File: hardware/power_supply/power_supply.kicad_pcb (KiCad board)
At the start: 2 copper layers, 163 x 130 mm, 168 parts, among them P101 XFRMR, P102 Clock board, P103 Rx #1, P104 Rx #2, P105 CPU board, Q201 IRLZ44N, Q202 BC547, Q203 BC557, Q301 IRFZ34N, Q302 IRF9Z34N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

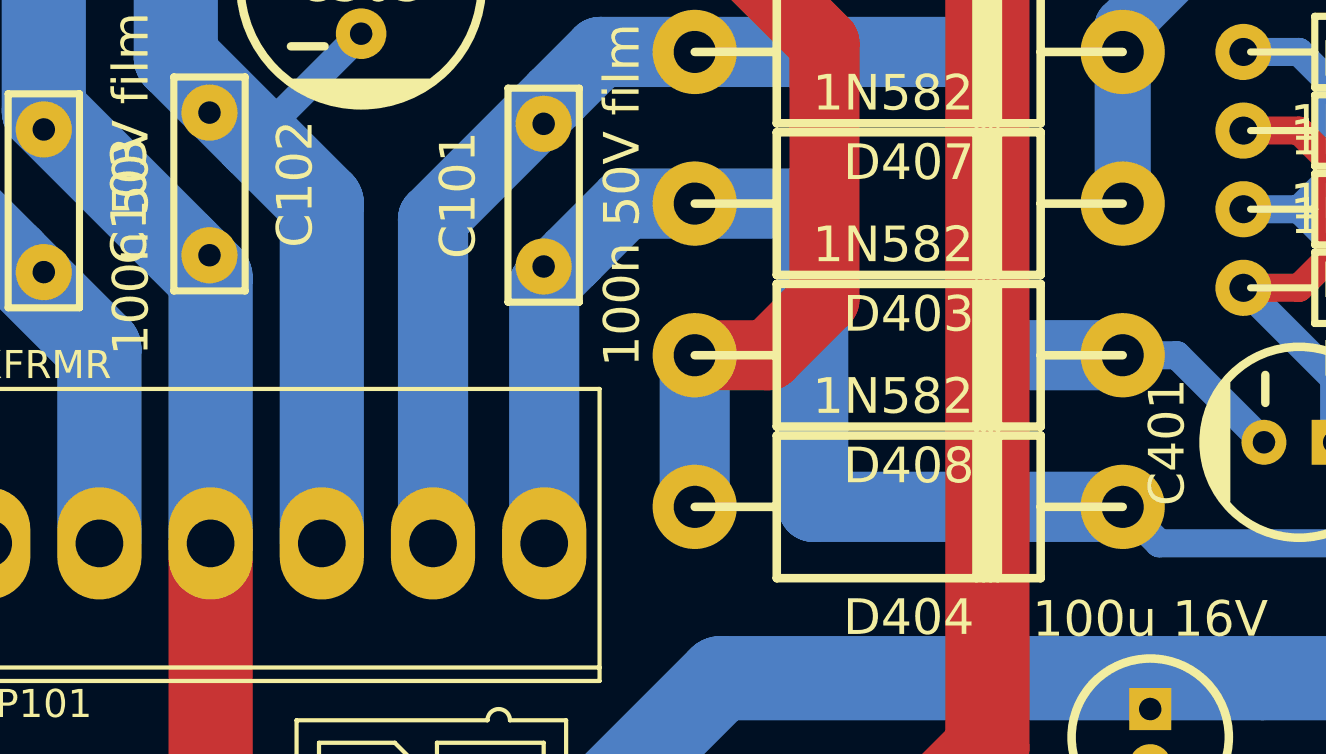
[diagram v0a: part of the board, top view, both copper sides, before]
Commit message: Update: PCB gerbers, images. Tagged v0.15
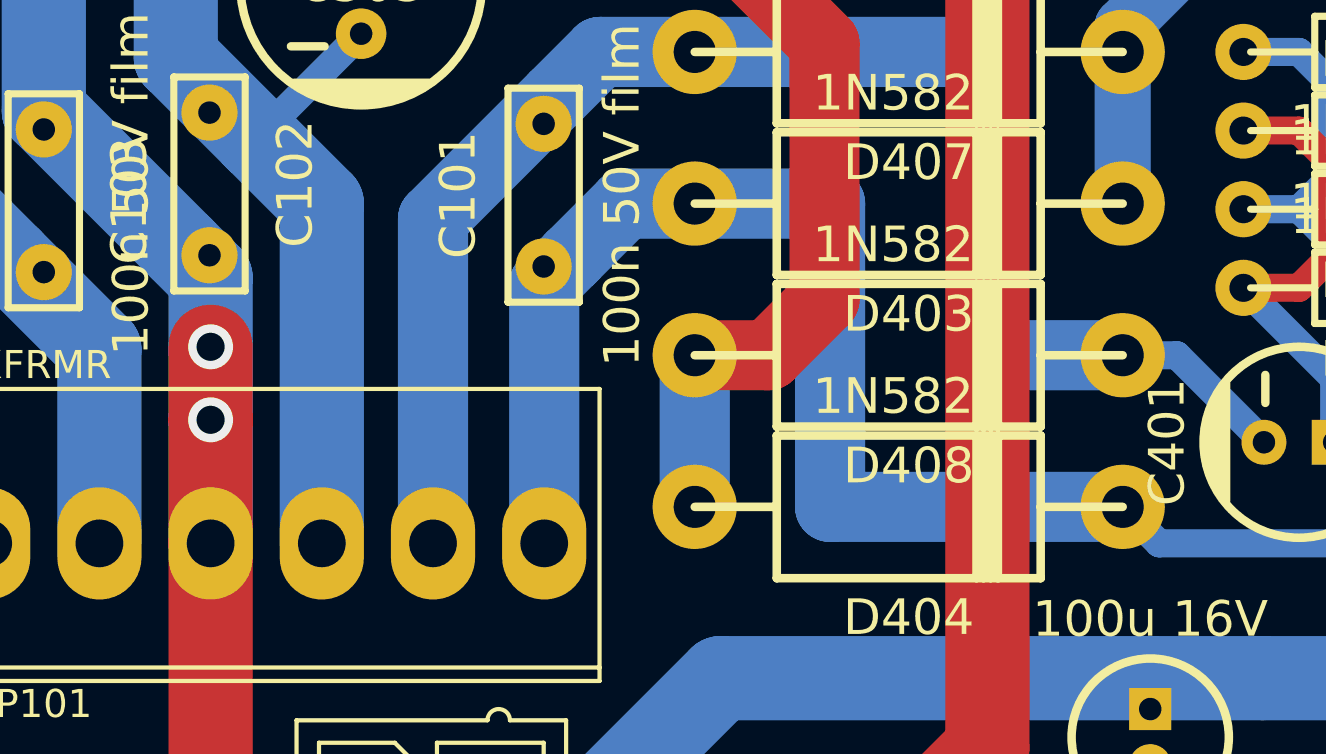
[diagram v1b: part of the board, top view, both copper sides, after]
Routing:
- net GND: track 622.4 -> 629.4 mm, vias 5 -> 7
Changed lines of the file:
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@@
     (thickness 1.6)
     (drawings 20)
-    (tracks 711)
+    (tracks 718)
     (zones 0)
     (modules 168)
@@
   )
   (setup
-    (last_trace_width 1)
+    (last_trace_width 3)
     (user_trace_width 0.8)
     (user_trace_width 1)
@@
     (visible_elements 7FFEF7FF)
     (pcbplotparams
-      (layerselection 3178497)
+      (layerselection 32769)
       (usegerberextensions false)
-      (excludeedgelayer true)
+      (excludeedgelayer false)
       (linewidth 0.150000)
       (plotframeref false)
@@
       (outputformat 4)
       (mirror false)
-      (drillshape 0)
+      (drillshape 2)
       (scaleselection 1)
       (outputdirectory pcb_plots/))
@@
   (segment (start 171.12 118.38) (end 172.1 117.4) (width 2.5) (layer B.Cu) (net 18))
   (segment (start 172.1 117.4) (end 174 115.5) (width 2.5) (layer B.Cu) (net 18))
-  (segment (start 176.48 115.5) (end 180.7 115.5) (width 2.5) (layer B.Cu) (net 18))
-  (segment (start 180.7 115.5) (end 180.7 126.3) (width 2.5) (layer B.Cu) (net 18))
-  (segment (start 180.7 126.3) (end 191.72 126.3) (width 2.5) (layer B.Cu) (net 18))
+  (segment (start 176.48 115.5) (end 181.3 115.5) (width 2.5) (layer B.Cu) (net 18))
+  (segment (start 181.3 115.5) (end 181.3 126.3) (width 2.5) (layer B.Cu) (net 18))
+  (segment (start 181.3 126.3) (end 191.72 126.3) (width 2.5) (layer B.Cu) (net 18))
   (segment (start 171.1 112.66) (end 171.5 112.26) (width 1) (layer B.Cu) (net 19))
   (segment (start 171.5 112.26) (end 171.5 111.7) (width 1) (layer B.Cu) (net 19))
@@
   (segment (start 171.5 111.7) (end 173.1 110.1) (width 2.5) (layer B.Cu) (net 19))
   (segment (start 176.48 110.1) (end 186.9 110.1) (width 2.5) (layer B.Cu) (net 19))
+  (segment (start 159.24 120.6) (end 159.24 123.2) (width 3) (layer F.Cu) (net 20))
+  (segment (start 159.24 123.2) (end 159.24 127.6) (width 3) (layer F.Cu) (net 20))
+  (via (at 159.24 120.6) (size 1.6) (drill 1) (layers F.Cu B.Cu) (net 20))
+  (segment (start 159.24 123.2) (end 159.24 127.6) (width 3) (layer B.Cu) (net 20))
+  (segment (start 159.24 120.7) (end 159.24 123.2) (width 3) (layer B.Cu) (net 20))
+  (segment (start 159.24 120.6) (end 159.24 120.7) (width 3) (layer B.Cu) (net 20))
+  (via (at 159.24 123.2) (size 1.6) (drill 1) (layers F.Cu B.Cu) (net 20))
+  (segment (start 159.24 118.14) (end 159.24 120.6) (width 3) (layer B.Cu) (net 20))
+  (segment (start 158.2 117.1) (end 159.24 118.14) (width 3) (layer B.Cu) (net 20))
   (segment (start 105.8 145) (end 109.3 145) (width 3) (layer B.Cu) (net 20))
   (segment (start 102.3 145) (end 105.8 145) (width 3) (layer B.Cu) (net 20))
@@
   (via (at 95.3 145) (size 1.6) (drill 1) (layers F.Cu B.Cu) (net 20))
   (segment (start 105.8 145) (end 102.3 145) (width 3) (layer F.Cu) (net 20))
-  (via (at 109.3 145) (size 1.6) (drill 1) (layers F.Cu B.Cu) (net 20) (status 1000000))
+  (via (at 109.3 145) (size 1.6) (drill 1) (layers F.Cu B.Cu) (net 20))
   (segment (start 105.8 145) (end 109.3 145) (width 3) (layer F.Cu) (net 20))
   (via (at 105.8 145) (size 1.6) (drill 1) (layers F.Cu B.Cu) (net 20))
@@
   (segment (start 158.96 117.1) (end 158.2 117.1) (width 1) (layer B.Cu) (net 20))
   (segment (start 153.3 112.2) (end 158.2 117.1) (width 3) (layer B.Cu) (net 20))
-  (segment (start 158.2 117.1) (end 159.24 118.14) (width 3) (layer B.Cu) (net 20))
   (segment (start 153.3 86.5) (end 153.3 112.2) (width 3) (layer B.Cu) (net 20))
-  (segment (start 159.24 118.14) (end 159.24 127.6) (width 3) (layer B.Cu) (net 20))
   (segment (start 181.78 96.4) (end 181.78 99.2) (width 1.5) (layer B.Cu) (net 20))
   (segment (start 191.1 96.3) (end 181.88 96.3) (width 1.5) (layer B.Cu) (net 20))
